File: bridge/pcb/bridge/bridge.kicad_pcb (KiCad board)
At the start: 2 copper layers, 163 x 83 mm, 30 parts, among them J1 Screw_Terminal_01x06, J2 Screw_Terminal_01x06, J3 Screw_Terminal_01x06, J4 Conn_01x23, Q1 PMOS, Q2 PMOS, Q3 PMOS, Q4 PMOS, Q5 PMOS, SW1 SW_SPST, U1 YAAJ_BluePill, U2 J104D2C12VDC.20S, U3 AD557JN

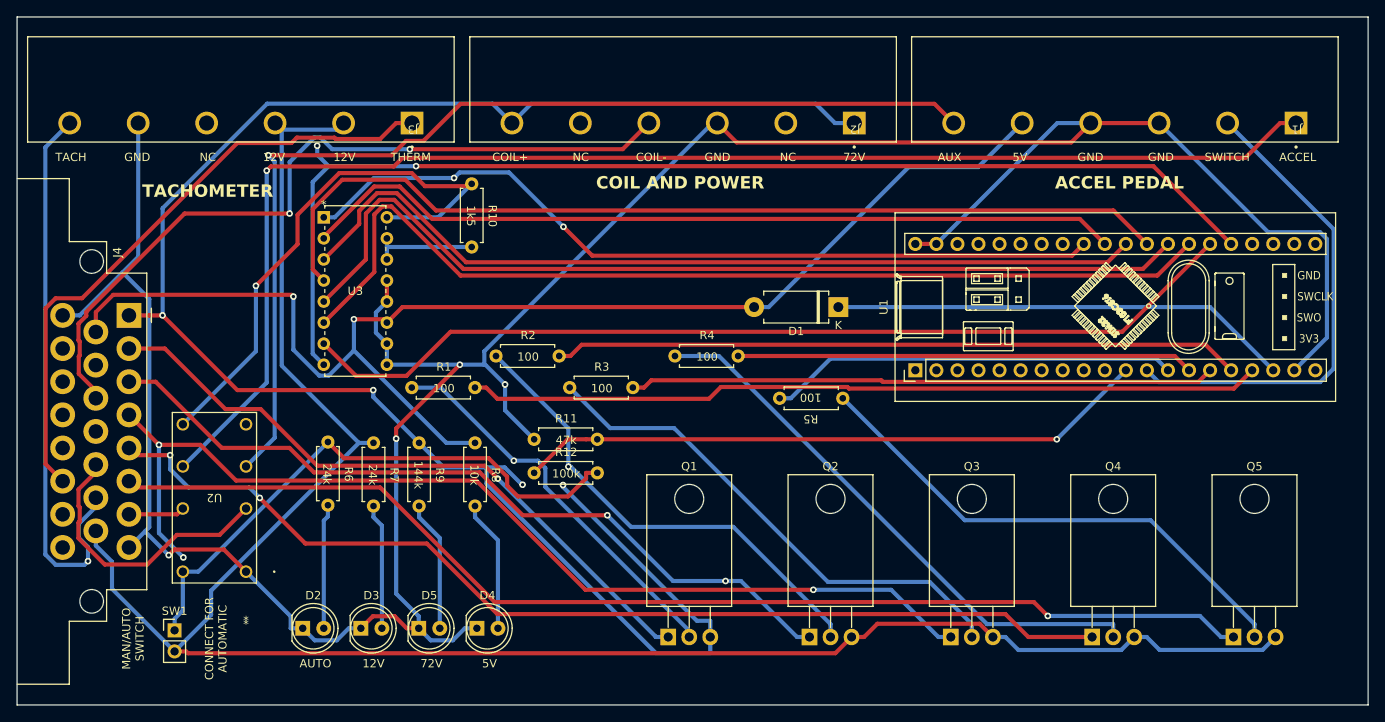
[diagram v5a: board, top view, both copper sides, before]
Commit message: Changed board size to make ordering cheaper
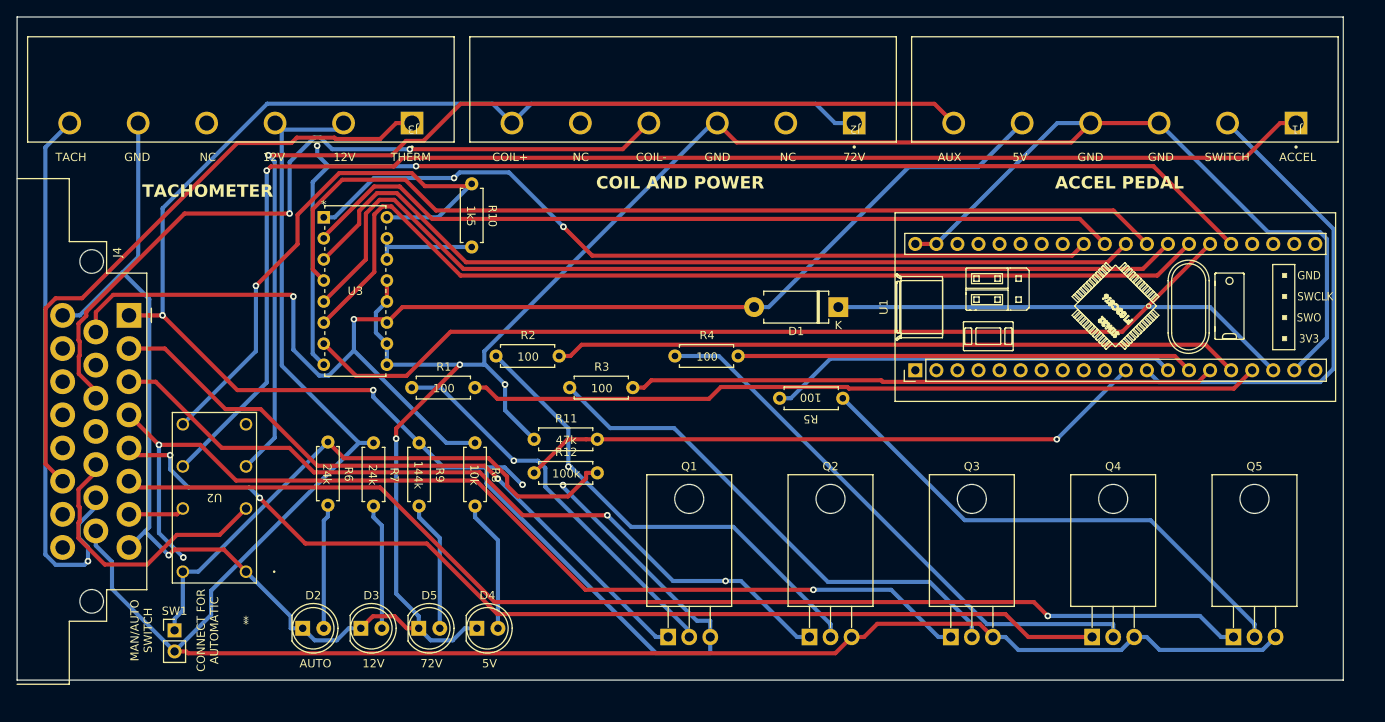
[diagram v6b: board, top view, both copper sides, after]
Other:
- board size 163 x 83 mm -> 160 x 80 mm
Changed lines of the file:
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@@
       (outputformat 1)
       (mirror false)
-      (drillshape 1)
+      (drillshape 0)
       (scaleselection 1)
-      (outputdirectory "")
+      (outputdirectory "~/Desktop")
     )
   )
@@
     )
   )
-  (gr_rect (start 63 41) (end 226 124)
+  (gr_rect (start 63 41) (end 223 121)
     (stroke (width 0.1) (type default)) (fill none) (layer "Edge.Cuts"))
   (gr_text "TACH" (at 69.5 58.5) (layer "F.SilkS")
@@
     (effects (font (size 1 1) (thickness 0.15)))
   )
-  (gr_text "MAN/AUTO\nSWITCH" (at 77 116 90) (layer "F.SilkS")
+  (gr_text "MAN/AUTO\nSWITCH" (at 78 115 90) (layer "F.SilkS")
     (effects (font (size 1 1) (thickness 0.15)))
   )
@@
     (effects (font (size 1 1) (thickness 0.15)) (justify bottom))
   )
-  (gr_text "CONNECT FOR\nAUTOMATIC" (at 87 116 90) (layer "F.SilkS")
+  (gr_text "CONNECT FOR\nAUTOMATIC" (at 86 115 90) (layer "F.SilkS")
     (effects (font (size 1 1) (thickness 0.15)))
   )
